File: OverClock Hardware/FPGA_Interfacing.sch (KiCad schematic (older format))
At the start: 8 parts

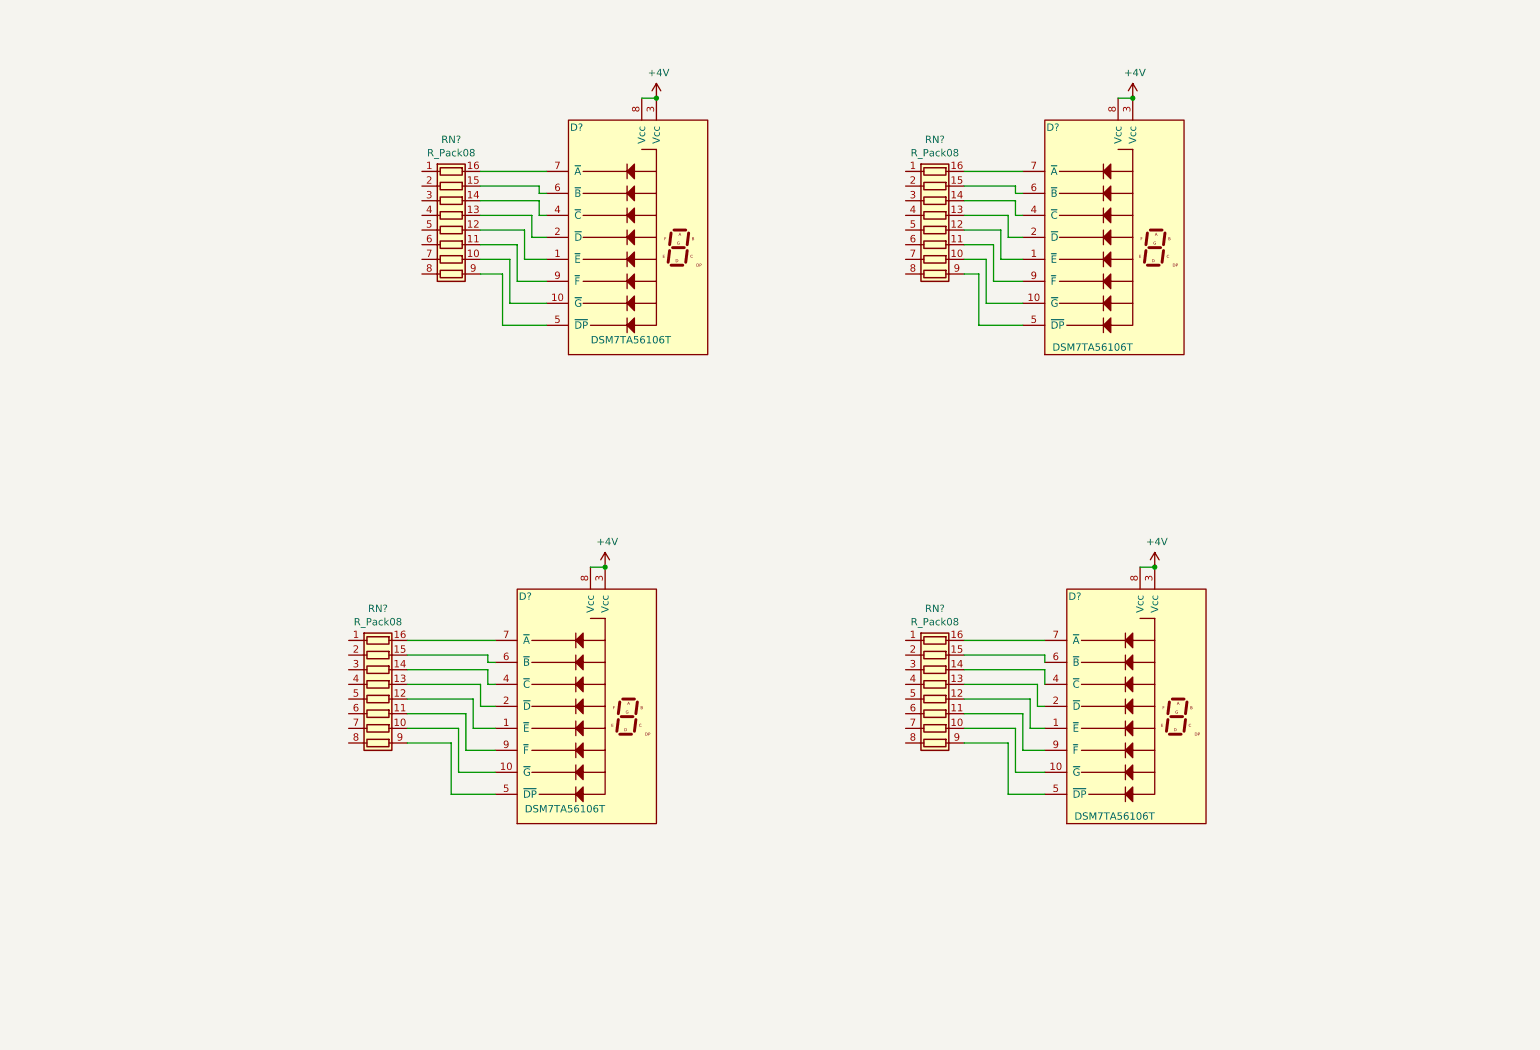
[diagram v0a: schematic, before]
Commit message: Added JTAG Header
Added a JTAG header and interfaced it to the FPGA as per: page 16 https://www.intel.com/content/dam/www/programmable/us/en/pdfs/literature/hb/max-10/m10_guidelines.pdf
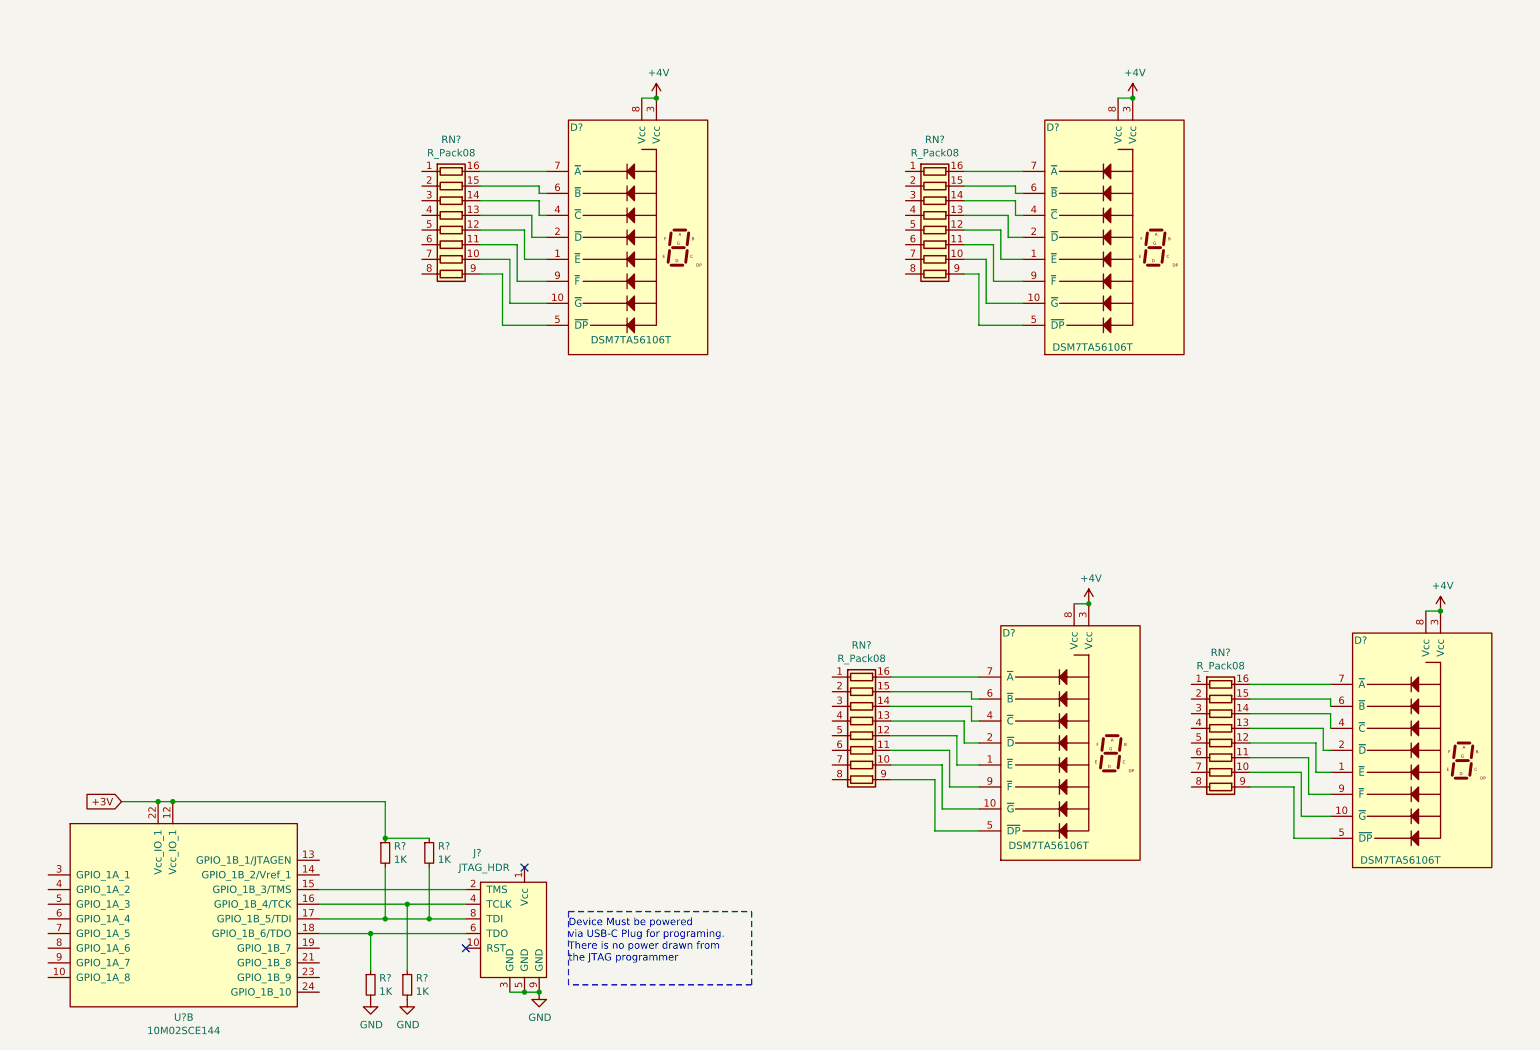
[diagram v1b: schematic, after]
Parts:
- added J?: JTAG_HDR, Connector_PinHeader_2.54mm:PinHeader_2x05_P2.54mm_Vertical, symbol Maxted_Libs:JTAG_HDR
- added R? (x4): 1K, symbol Device:R_Small
- added U?: 10M02SCE144, Maxted Libs:QFP-144_EPAD_20x20_Pitch0.5mm, symbol Maxted_Libs:10M02SCE144
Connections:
- new net: J?.2 (TMS), U?.15 (GPIO_1B_3/TMS)
- new net: J?.4 (TCLK), R?.1, U?.16 (GPIO_1B_4/TCK)
- new net: J?.8 (TDI), R?.2, R?.2, U?.17 (GPIO_1B_5/TDI)
- new net: J?.6 (TDO), R?.1, U?.18 (GPIO_1B_6/TDO)
- new net +3V: R?.1, R?.1, U?.12 (Vcc_IO_1), U?.22 (Vcc_IO_1)
- new net GND: J?.3 (GND), J?.5 (GND), J?.9 (GND), R?.2, R?.2
- no-connect marks 0 -> 2
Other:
- note added: "Device Must be powered \nvia USB-C Plug for programing.\nThere is no power drawn from\nthe JTAG programmer\n"
- moved on the sheet: D?, RN?

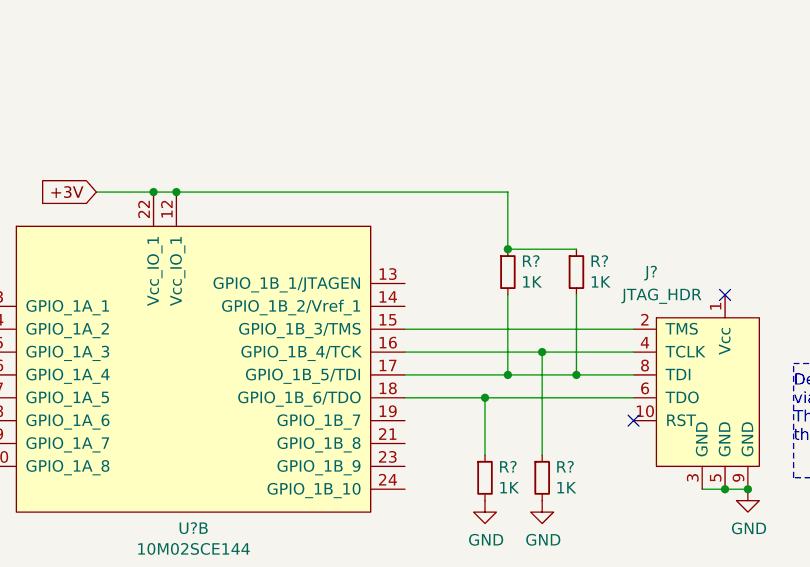
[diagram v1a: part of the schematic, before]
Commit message: Fix duplicate Pullup Resistor on JTAG Header.
Fixed error in JTAG header pullup resistor where the TDI line had 2 pullups and teh TMS had none. Both pins now have one each.
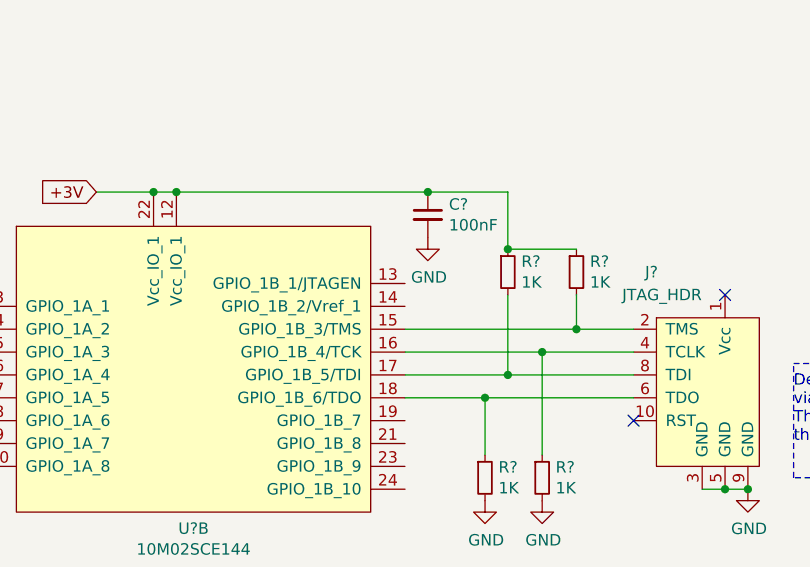
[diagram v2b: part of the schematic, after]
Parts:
- added C?: 100nF, symbol Device:C_Small
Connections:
- net +3V: now also C?.1
- net GND: now also C?.2
- net at J?.2 (TMS), U?.15 (GPIO_1B_3/TMS): now also R?.2
- net at J?.8 (TDI), R?.2, U?.17 (GPIO_1B_5/TDI): no longer R?.2
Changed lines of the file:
@@
 +3V
 Wire Wire Line
-	3700 6700 3450 6700
-Wire Wire Line
-	2700 6600 3300 6600
-Wire Wire Line
-	2700 6500 3700 6500
+	2700 6500 3450 6500
 $Comp
 L Device:R_Small R?
@@
 $EndComp
 Wire Wire Line
-	2700 6800 3050 6800
-Wire Wire Line
 	3050 6800 3050 7050
-Connection ~ 3050 6800
-Wire Wire Line
-	3050 6800 3700 6800
 Wire Wire Line
 	3300 6600 3300 7050
-Connection ~ 3300 6600
-Wire Wire Line
-	3300 6600 3700 6600
 $Comp
 L Device:R_Small R?
@@
 Wire Wire Line
 	3150 6700 3150 6350
-Connection ~ 3150 6700
-Wire Wire Line
-	3150 6700 2700 6700
-Wire Wire Line
-	3450 6700 3450 6350
-Connection ~ 3450 6700
-Wire Wire Line
-	3450 6700 3150 6700
 $Comp
 L Device:R_Small R?
@@
 $EndComp
 Wire Wire Line
-	1700 5900 3150 5900
+	1700 5900 2800 5900
 Wire Wire Line
 	3150 5900 3150 6150
@@
 Wire Notes Line style solid rgb(0, 0, 0)
 	4400 7150 4400 6650
+$Comp
+L Device:C_Small C?
+U 1 1 5C6B33C4
+P 2800 6000
+F 0 "C?" H 2892 6046 50  0000 L CNN
+F 1 "100nF" H 2892 5955 50  0000 L CNN
+F 2 "" H 2800 6000 50  0001 C CNN
+F 3 "~" H 2800 6000 50  0001 C CNN
+	1    2800 6000
+	1    0    0    -1
+$EndComp
+Connection ~ 2800 5900
+Wire Wire Line
+	2800 5900 3150 5900
+Connection ~ 3300 6600
+Connection ~ 3050 6800
+Wire Wire Line
+	3050 6800 3700 6800
+Wire Wire Line
+	2700 6800 3050 6800
+Wire Wire Line
+	3300 6600 3700 6600
+Wire Wire Line
+	2700 6600 3300 6600
+Wire Wire Line
+	3150 6700 2700 6700
+Connection ~ 3150 6700
+$Comp
+L power:GND #PWR?
+U 1 1 5C6B34AA
+P 2800 6100
+F 0 "#PWR?" H 2800 5850 50  0001 C CNN
+F 1 "GND" H 2805 5927 50  0000 C CNN
+F 2 "" H 2800 6100 50  0001 C CNN
+F 3 "" H 2800 6100 50  0001 C CNN
+	1    2800 6100
+	1    0    0    -1
+$EndComp
+Wire Wire Line
+	3150 6700 3700 6700
+Wire Wire Line
+	3450 6500 3450 6350
+Connection ~ 3450 6500
+Wire Wire Line
+	3450 6500 3700 6500
 $EndSCHEMATC

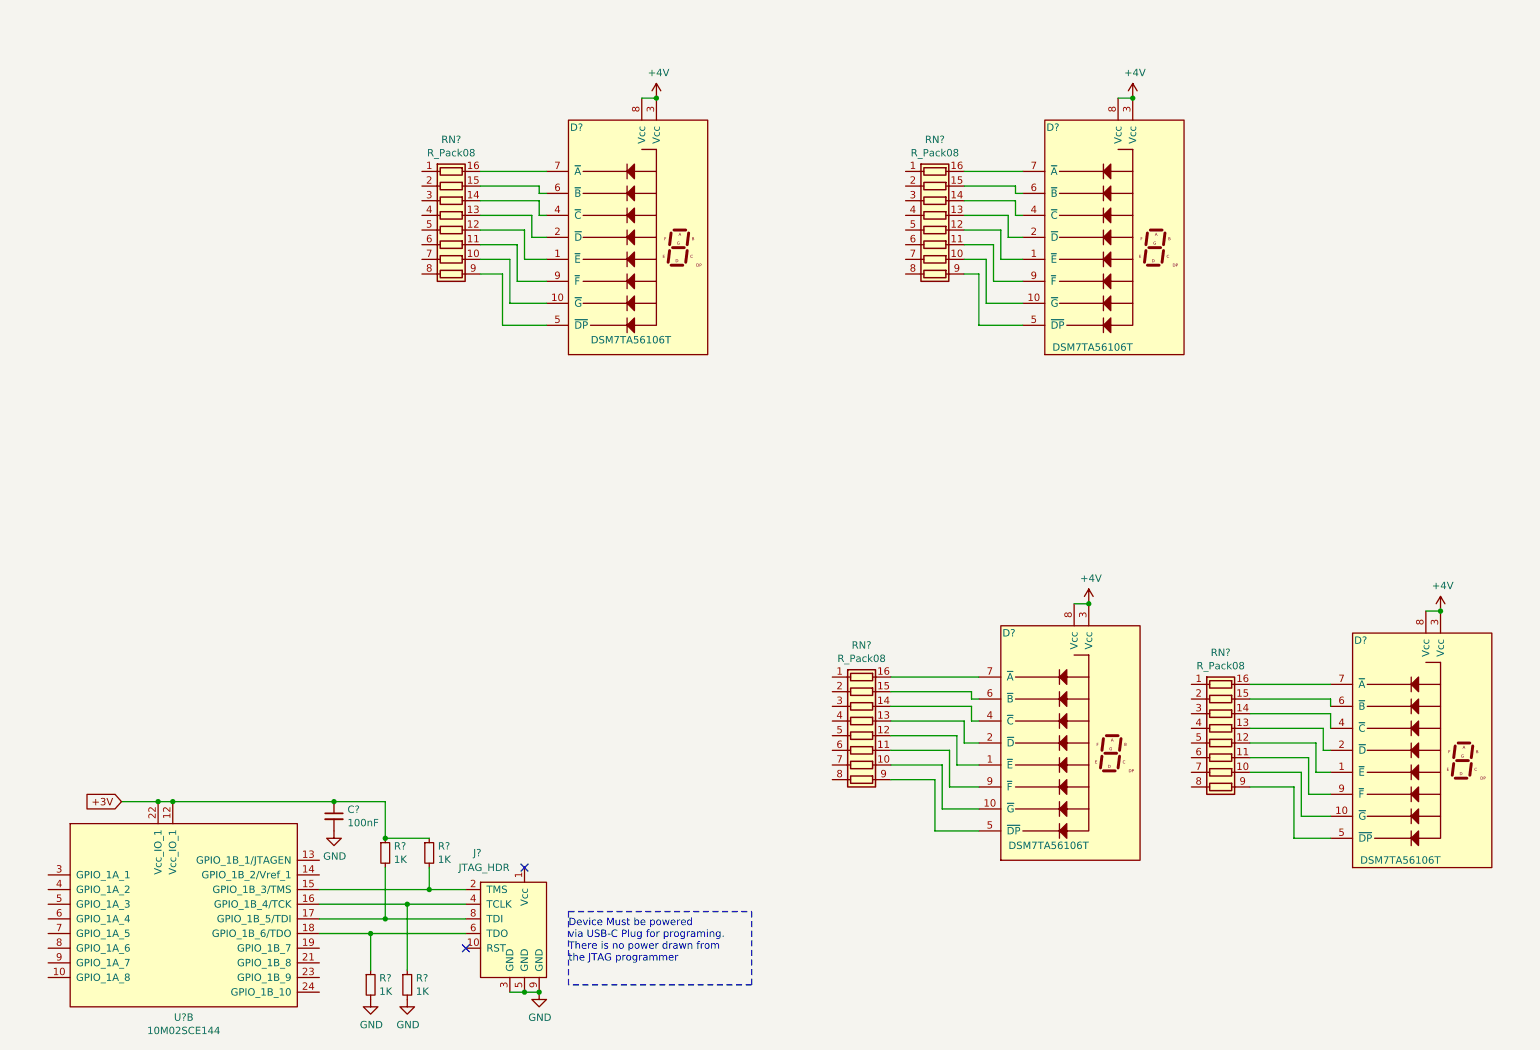
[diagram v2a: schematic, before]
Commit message: Added Decoupling strategy and started adding decoupling capacitors
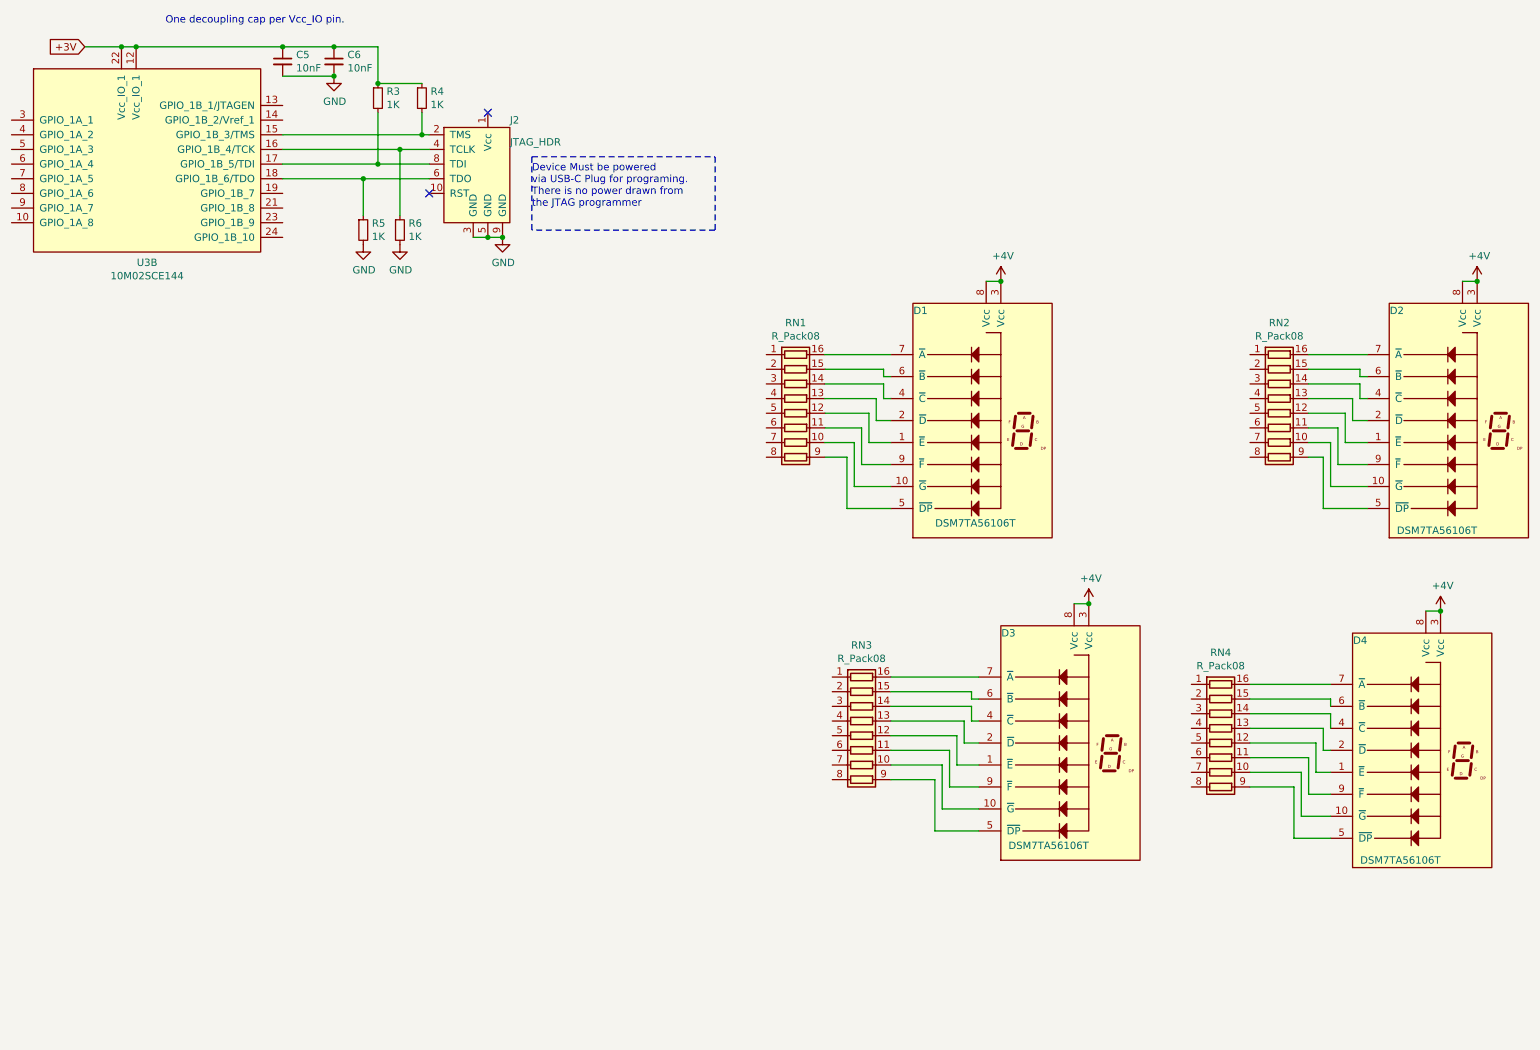
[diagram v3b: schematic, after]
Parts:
- added C6: 10nF, symbol Device:C_Small
- C5: renamed from C?; value 100nF -> 10nF
- gave numbers to parts that had none: 14
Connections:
- net +3V: now also C6.1
- net GND: now also C6.2
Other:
- note added: "One decoupling cap per Vcc_IO pin."
- moved on the sheet: C5, D1, D2, J2, R3, R4, R5, R6, RN1, RN2, U3B
